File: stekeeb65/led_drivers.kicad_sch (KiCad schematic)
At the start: 28 parts, among them IC1 IS31FL3733B-TQLS4, IC2 IS31FL3733B-TQLS4

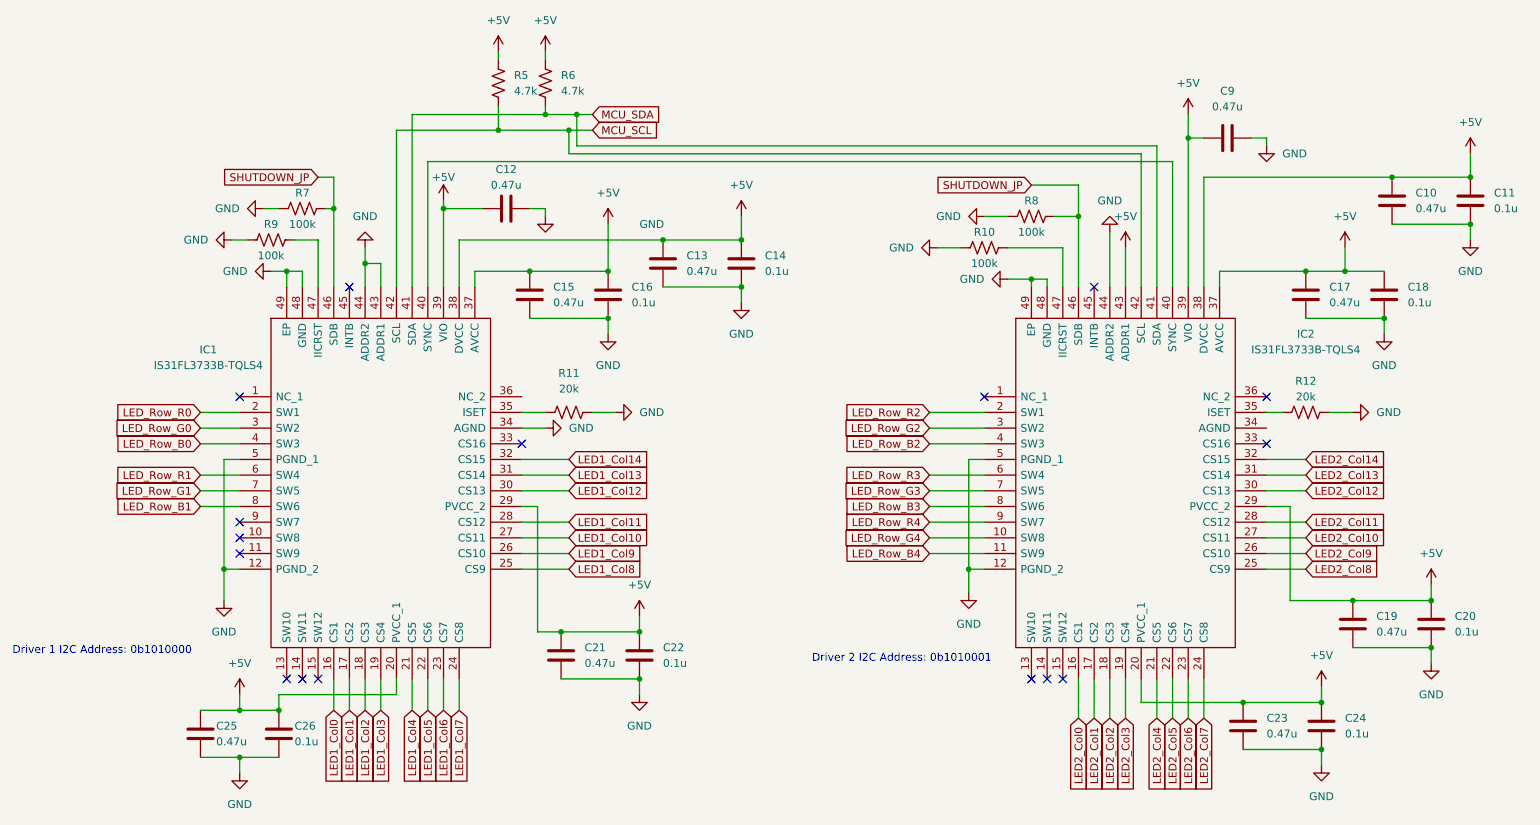
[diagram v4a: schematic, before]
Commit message: Redoing keyboard layout. Adding flex cuts to PCB
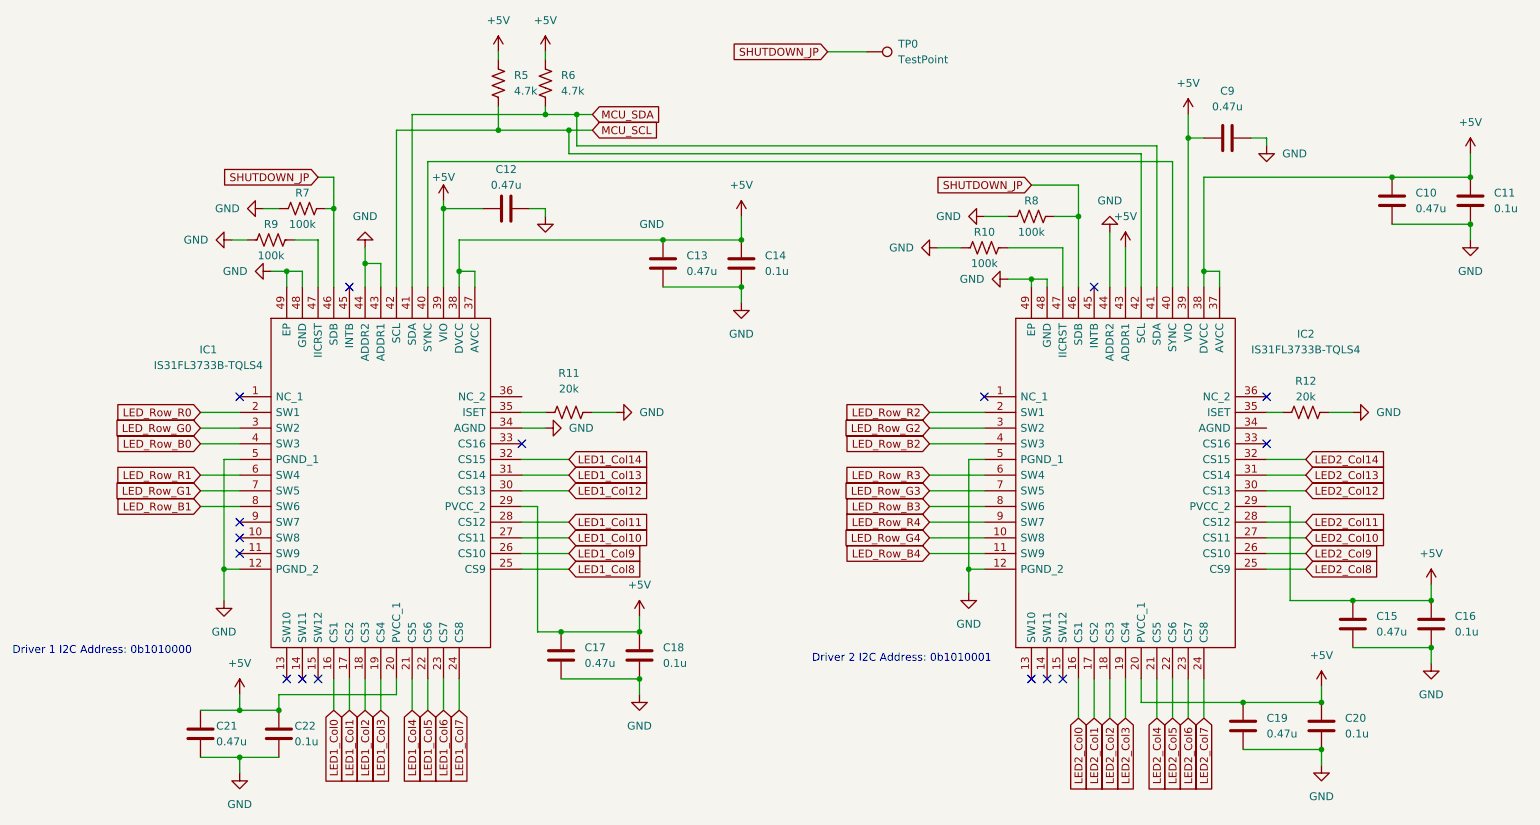
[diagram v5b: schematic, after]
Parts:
- removed C15, C17: 0.47u, Capacitor_SMD:C_0603_1608Metric_Pad1.08x0.95mm_HandSolder, symbol Device:C
- removed C16, C18: 0.1u, Capacitor_SMD:C_0603_1608Metric_Pad1.08x0.95mm_HandSolder, symbol Device:C
- added TP0: TestPoint, TestPoint:TestPoint_Pad_D1.0mm, symbol Connector:TestPoint
- renumbered C19 to C15, C20 to C16, C21 to C17, C22 to C18, C23 to C19, C24 to C20, C25 to C21, C26 to C22
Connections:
- net SHUTDOWN_JP: now also TP0.1

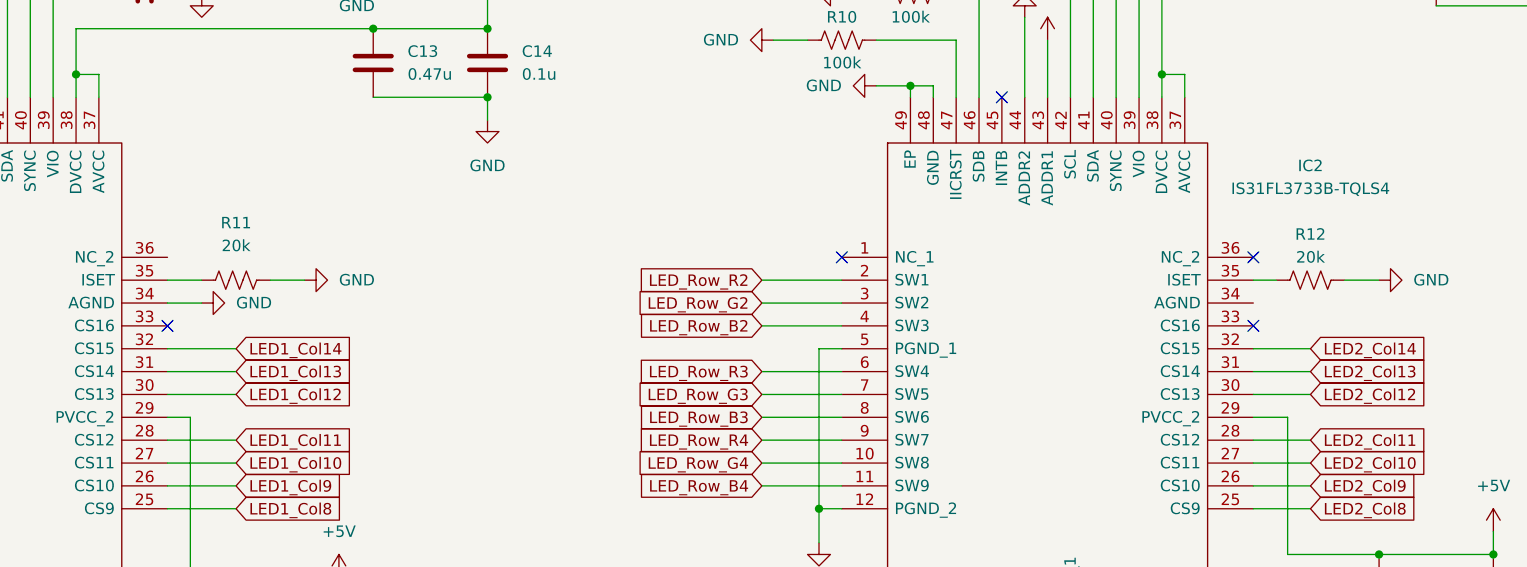
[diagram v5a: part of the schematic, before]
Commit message: Replacing Type-C in lieu of a daughter board connector.
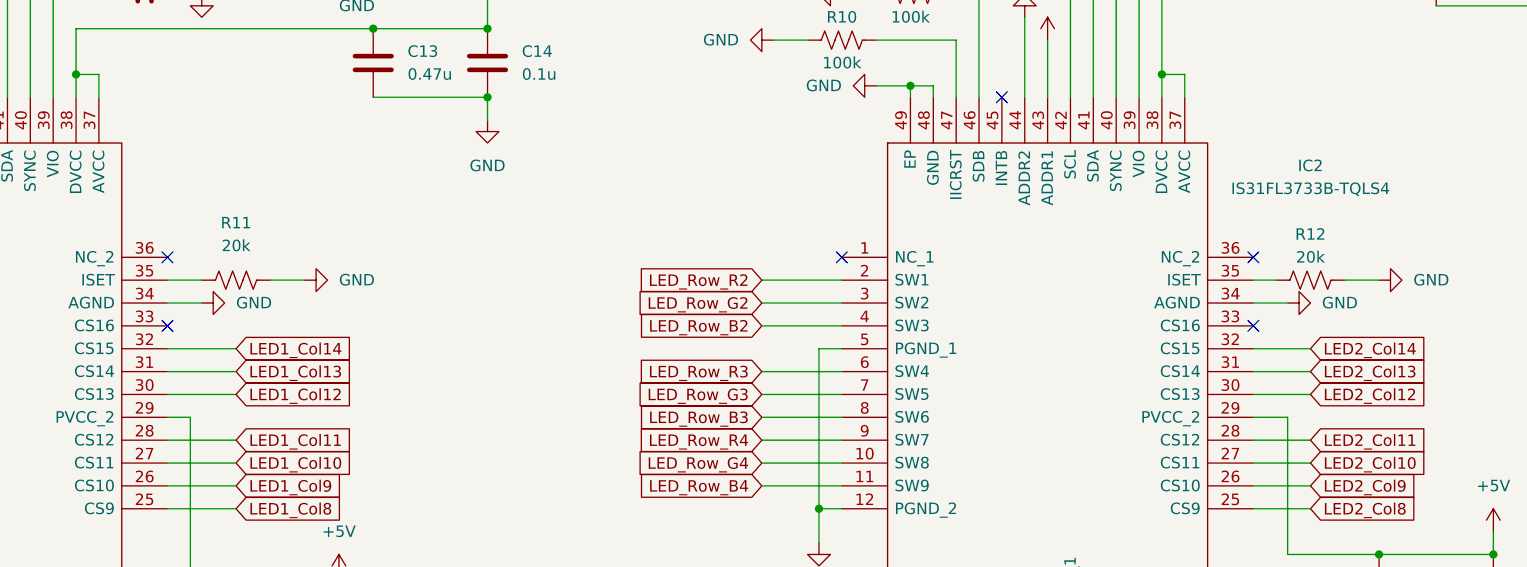
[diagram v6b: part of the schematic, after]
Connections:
- net GND: now also IC2.34 (AGND)
- no-connect marks 16 -> 17
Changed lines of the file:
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@@
   (no_connect (at 58.42 99.06))
   (no_connect (at 58.42 101.6))
+  (no_connect (at 104.14 76.2))
   (no_connect (at 58.42 76.2))
   (no_connect (at 186.69 121.92))
@@
   )
   (wire (pts (xy 127 58.42) (xy 139.7 58.42))
+    (stroke (width 0) (type default) (color 0 0 0 0))
+  )
+  (wire (pts (xy 224.79 81.28) (xy 228.6 81.28))
     (stroke (width 0) (type default) (color 0 0 0 0))
   )
@@
       (effects (font (size 1.27 1.27)) hide)
     )
+    (pin "1")
+  )
+  (symbol (lib_id "power:GND") (at 228.6 81.28 90) (unit 1)
+    (in_bom yes) (on_board yes) (fields_autoplaced)
+    (property "Reference" "#PWR0103" (id 0) (at 234.95 81.28 0)
+      (effects (font (size 1.27 1.27)) hide)
+    )
+    (property "Value" "GND" (id 1) (at 232.41 81.2799 90)
+      (effects (font (size 1.27 1.27)) (justify right))
+    )
+    (property "Footprint" "" (id 2) (at 228.6 81.28 0)
+      (effects (font (size 1.27 1.27)) hide)
+    )
+    (property "Datasheet" "" (id 3) (at 228.6 81.28 0)
+      (effects (font (size 1.27 1.27)) hide)
+    )
